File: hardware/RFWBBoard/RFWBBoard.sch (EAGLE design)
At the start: 122 parts, among them IC1 24LC025ST, J1 CON-71742-3003-BOT, M1 MOUNT-HOLE3.3, M2 MOUNT-HOLE3.3, M3 MOUNT-HOLE3.3, M4 MOUNT-HOLE3.3, M5 FIDUCIAL1X2, M6 FIDUCIAL1X2, M7 FIDUCIAL1X2, M8 FIDUCIAL1X2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

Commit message: - Logos - Gerber files - Pick and Place file - Assembly files
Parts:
- removed LOGO1: LOGO-ISIS-600MIL-10MM-AU, Logo:LOGO-ISIS-600MIL-10MM-AU
- removed LOGO2: LOGO-MARMOTE-600MIL-10MM-AU, Logo:LOGO-MARMOTE-600MIL-10MM-AU
- removed LOGO3: LOGO-VANDERBILT-600MIL-10MM-AU, Logo:LOGO-VANDERBILT-600MIL-10MM-AU
- added LOGO4: LOGO-ISIS-600MIL-10MM-SS, Logo:LOGO-ISIS-600MIL-10MM-SS
- added LOGO5: LOGO-VANDERBILT-600MIL-10MM-SS, Logo:LOGO-VANDERBILT-600MIL-10MM-SS
- added LOGO6: LOGO-MARMOTE-600MIL-10MM-SS, Logo:LOGO-MARMOTE-600MIL-10MM-SS
- added LOGO7: LOGO-RADIO-3-600MIL-10MM-SS, Logo:LOGO-RADIO-3-600MIL-10MM-SS
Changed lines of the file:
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@@
 <attribute name="REVIEWEREMAIL2" value="sandor.szilvasi@vanderbilt.edu"/>
 <attribute name="REVISION" value="A"/>
-<attribute name="TITLE" value="Radio Front-End Board"/>
+<attribute name="TITLE" value="Joshua"/>
 </attributes>
 <variantdefs>
@@
 <part name="RA00" library="RFWBBoard" deviceset="R" device="0402" value="DNP"/>
 <part name="RA01" library="RFWBBoard" deviceset="R" device="0402" value="DNP"/>
-<part name="LOGO1" library="Logo" deviceset="LOGO-ISIS-600MIL" device="-10MM-AU"/>
-<part name="LOGO2" library="Logo" deviceset="LOGO-MARMOTE-600MIL" device="-10MM-AU"/>
-<part name="LOGO3" library="Logo" deviceset="LOGO-VANDERBILT-600MIL" device="-10MM-AU"/>
 <part name="R1" library="RFWBBoard" deviceset="R" device="0402" value="4.7k"/>
 <part name="R2" library="RFWBBoard" deviceset="R" device="0402" value="4.7k"/>
@@
 <part name="C73" library="RFWBBoard" deviceset="C" device="0402" value="10nF"/>
 <part name="C71" library="RFWBBoard" deviceset="CPOL" device="2012" value="10uF"/>
+<part name="LOGO4" library="Logo" deviceset="LOGO-ISIS-600MIL" device="-10MM-SS"/>
+<part name="LOGO5" library="Logo" deviceset="LOGO-VANDERBILT-600MIL" device="-10MM-SS"/>
+<part name="LOGO6" library="Logo" deviceset="LOGO-MARMOTE-600MIL" device="-10MM-SS"/>
+<part name="LOGO7" library="Logo" deviceset="LOGO-RADIO-3-600MIL" device="-10MM-SS"/>
 </parts>
 <sheets>
 <sheet>
 <plain>
-<text x="53.34" y="116.84" size="10.16" layer="97">&gt;TITLE</text>
+<text x="99.06" y="116.84" size="10.16" layer="97">&gt;TITLE</text>
 <text x="38.1" y="101.6" size="5.08" layer="97">7.5-18 MHz wide 2.4-2.5 GHz/Baseband Radio Front-End</text>
 <text x="74.93" y="81.28" size="5.08" layer="97">http://marmote.googlecode.com</text>
@@
 <instance part="U$1" gate="G$1" x="0" y="0"/>
 <instance part="U$2" gate="G$1" x="81.28" y="0"/>
-<instance part="LOGO1" gate="G$1" x="119.38" y="53.34"/>
-<instance part="LOGO2" gate="G$1" x="152.4" y="53.34"/>
-<instance part="LOGO3" gate="G$1" x="86.36" y="53.34"/>
+<instance part="LOGO4" gate="G$1" x="104.14" y="53.34"/>
+<instance part="LOGO5" gate="G$1" x="73.66" y="53.34"/>
+<instance part="LOGO6" gate="G$1" x="134.62" y="53.34"/>
+<instance part="LOGO7" gate="G$1" x="165.1" y="53.34"/>
 </instances>
 <busses>

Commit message: - Gerber - BOM - README.txt - Schematic
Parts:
- C104: value NONE -> DNP
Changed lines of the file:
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@@
 <layer number="196" name="mValues" color="7" fill="1" visible="no" active="no"/>
 <layer number="199" name="EXTD_ERC" color="7" fill="1" visible="yes" active="yes"/>
-<layer number="200" name="200bmp" color="1" fill="10" visible="yes" active="yes"/>
+<layer number="200" name="200bmp" color="1" fill="10" visible="no" active="yes"/>
 <layer number="201" name="201bmp" color="2" fill="10" visible="yes" active="yes"/>
 <layer number="202" name="202bmp" color="3" fill="10" visible="yes" active="yes"/>
@@
 <part name="C103" library="RFWBBoard" deviceset="C" device="0402" value="100pF"/>
 <part name="C117" library="RFWBBoard" deviceset="C" device="0402" value="100nF"/>
-<part name="C104" library="RFWBBoard" deviceset="C" device="0402" value="NONE"/>
+<part name="C104" library="RFWBBoard" deviceset="C" device="0402" value="DNP"/>
 <part name="C106" library="RFWBBoard" deviceset="C" device="0402" value="100pF"/>
 <part name="C107" library="RFWBBoard" deviceset="C" device="0402" value="100pF"/>

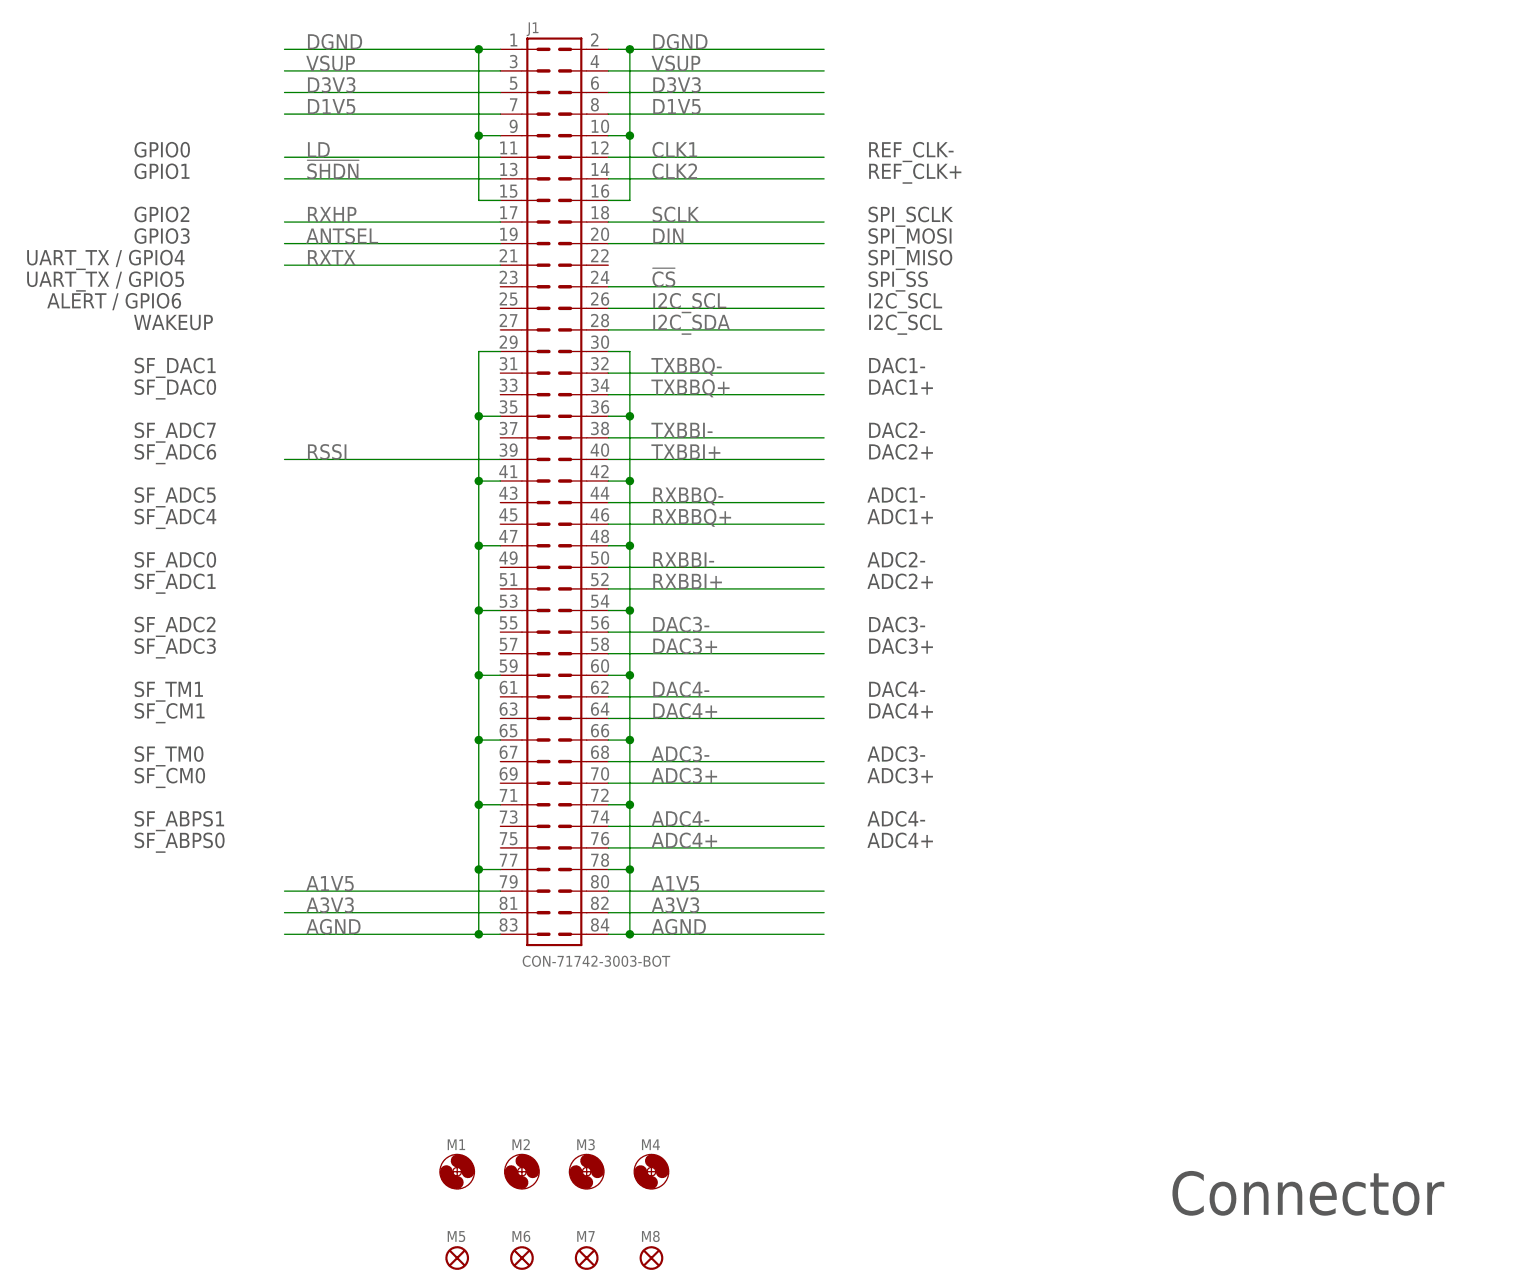
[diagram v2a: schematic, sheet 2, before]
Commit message: Modified signal name notes around connector.
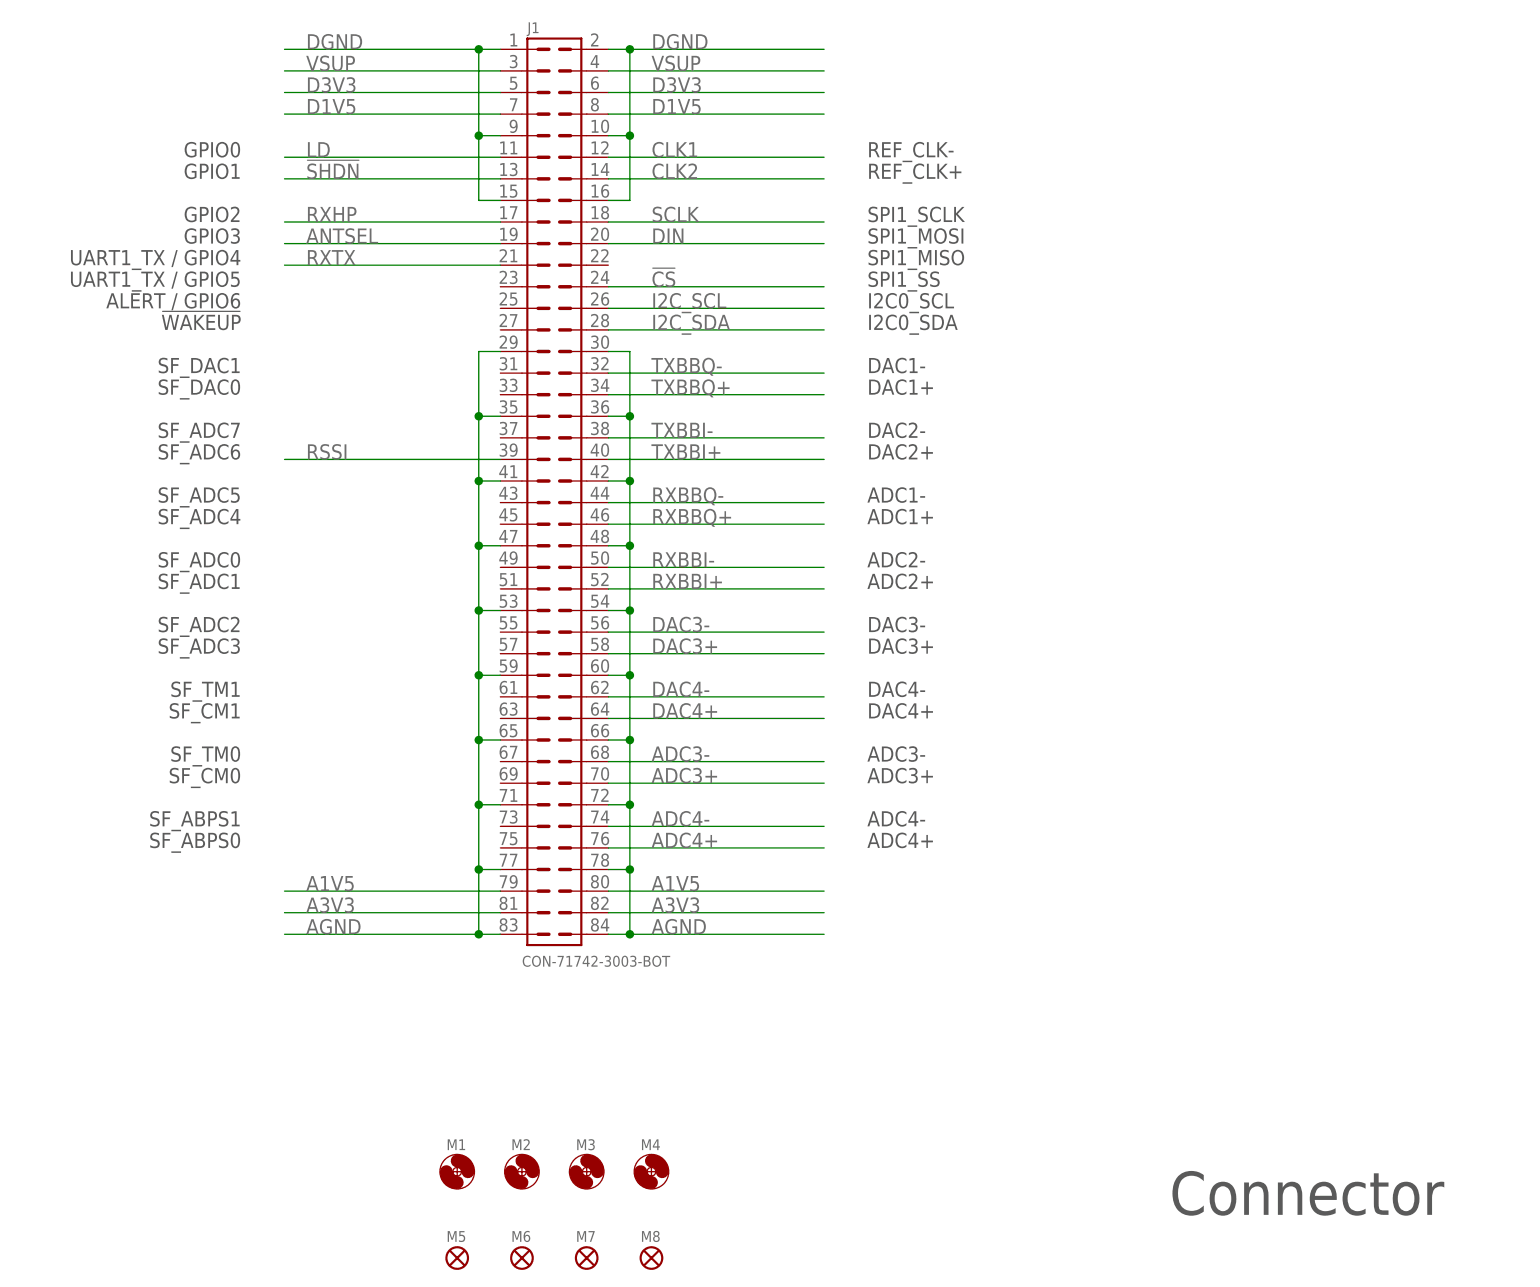
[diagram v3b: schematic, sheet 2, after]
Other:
- note added: "!WAKEUP"
- note added: "I2C0_SCL"
- note added: "I2C0_SDA"
- note added: "SPI1_MISO"
- note added: "SPI1_MOSI"
- note added: "SPI1_SCLK"
- note added: "SPI1_SS"
- note added: "UART1_TX / GPIO4"
- note added: "UART1_TX / GPIO5"
- note removed: "I2C_SCL"
- note removed: "SPI_MISO"
- note removed: "SPI_MOSI"
- note removed: "SPI_SCLK"
- note removed: "SPI_SS"
- note removed: "UART_TX / GPIO4"
- note removed: "UART_TX / GPIO5"
- note removed: "WAKEUP"
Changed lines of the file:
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@@
 <setting verticaltext="up"/>
 </settings>
-<grid distance="0.1" unitdist="inch" unit="inch" style="lines" multiple="1" display="no" altdistance="0.05" altunitdist="inch" altunit="inch"/>
+<grid distance="0.1" unitdist="inch" unit="inch" style="lines" multiple="1" display="no" altdistance="0.025" altunitdist="inch" altunit="inch"/>
 <layers>
 <layer number="1" name="Top" color="4" fill="1" visible="no" active="no"/>
@@
 <plain>
 <text x="190.5" y="20.32" size="5.08" layer="97">&gt;PAGE2</text>
-<text x="68.58" y="109.22" size="1.778" layer="97">SF_ADC6</text>
-<text x="68.58" y="137.16" size="1.778" layer="97">GPIO2</text>
-<text x="68.58" y="134.62" size="1.778" layer="97">GPIO3</text>
-<text x="68.58" y="142.24" size="1.778" layer="97">GPIO1</text>
-<text x="68.58" y="144.78" size="1.778" layer="97">GPIO0</text>
-<text x="55.88" y="132.08" size="1.778" layer="97">UART_TX / GPIO4</text>
-<text x="154.94" y="137.16" size="1.778" layer="97">SPI_SCLK</text>
-<text x="154.94" y="134.62" size="1.778" layer="97">SPI_MOSI</text>
-<text x="154.94" y="132.08" size="1.778" layer="97">SPI_MISO</text>
-<text x="154.94" y="129.54" size="1.778" layer="97">SPI_SS</text>
-<text x="154.94" y="127" size="1.778" layer="97">I2C_SCL</text>
-<text x="154.94" y="124.46" size="1.778" layer="97">I2C_SCL</text>
+<text x="81.28" y="109.22" size="1.778" layer="97" rot="MR0">SF_ADC6</text>
+<text x="81.28" y="137.16" size="1.778" layer="97" rot="MR0">GPIO2</text>
+<text x="81.28" y="134.62" size="1.778" layer="97" rot="MR0">GPIO3</text>
+<text x="81.28" y="142.24" size="1.778" layer="97" rot="MR0">GPIO1</text>
+<text x="81.28" y="144.78" size="1.778" layer="97" rot="MR0">GPIO0</text>
+<text x="81.28" y="132.08" size="1.778" layer="97" rot="MR0">UART1_TX / GPIO4</text>
+<text x="154.94" y="137.16" size="1.778" layer="97">SPI1_SCLK</text>
+<text x="154.94" y="134.62" size="1.778" layer="97">SPI1_MOSI</text>
+<text x="154.94" y="132.08" size="1.778" layer="97">SPI1_MISO</text>
+<text x="154.94" y="129.54" size="1.778" layer="97">SPI1_SS</text>
+<text x="154.94" y="127" size="1.778" layer="97">I2C0_SCL</text>
+<text x="154.94" y="124.46" size="1.778" layer="97">I2C0_SDA</text>
 <text x="154.94" y="119.38" size="1.778" layer="97">DAC1-</text>
 <text x="154.94" y="116.84" size="1.778" layer="97">DAC1+</text>
@@
 <text x="154.94" y="144.78" size="1.778" layer="97">REF_CLK-</text>
 <text x="154.94" y="142.24" size="1.778" layer="97">REF_CLK+</text>
-<text x="55.88" y="129.54" size="1.778" layer="97">UART_TX / GPIO5</text>
-<text x="58.42" y="127" size="1.778" layer="97">ALERT / GPIO6</text>
-<text x="68.58" y="124.46" size="1.778" layer="97">WAKEUP</text>
-<text x="68.58" y="111.76" size="1.778" layer="97">SF_ADC7</text>
-<text x="68.58" y="119.38" size="1.778" layer="97">SF_DAC1</text>
-<text x="68.58" y="116.84" size="1.778" layer="97">SF_DAC0</text>
-<text x="68.58" y="104.14" size="1.778" layer="97">SF_ADC5</text>
-<text x="68.58" y="101.6" size="1.778" layer="97">SF_ADC4</text>
-<text x="68.58" y="96.52" size="1.778" layer="97">SF_ADC0</text>
-<text x="68.58" y="93.98" size="1.778" layer="97">SF_ADC1</text>
-<text x="68.58" y="88.9" size="1.778" layer="97">SF_ADC2</text>
-<text x="68.58" y="86.36" size="1.778" layer="97">SF_ADC3</text>
-<text x="68.58" y="81.28" size="1.778" layer="97">SF_TM1</text>
-<text x="68.58" y="78.74" size="1.778" layer="97">SF_CM1</text>
-<text x="68.58" y="73.66" size="1.778" layer="97">SF_TM0</text>
-<text x="68.58" y="71.12" size="1.778" layer="97">SF_CM0</text>
-<text x="68.58" y="66.04" size="1.778" layer="97">SF_ABPS1</text>
-<text x="68.58" y="63.5" size="1.778" layer="97">SF_ABPS0</text>
+<text x="81.28" y="129.54" size="1.778" layer="97" rot="MR0">UART1_TX / GPIO5</text>
+<text x="81.28" y="127" size="1.778" layer="97" rot="MR0">ALERT / GPIO6</text>
+<text x="81.28" y="124.46" size="1.778" layer="97" rot="MR0">!WAKEUP</text>
+<text x="81.28" y="111.76" size="1.778" layer="97" rot="MR0">SF_ADC7</text>
+<text x="81.28" y="119.38" size="1.778" layer="97" rot="MR0">SF_DAC1</text>
+<text x="81.28" y="116.84" size="1.778" layer="97" rot="MR0">SF_DAC0</text>
+<text x="81.28" y="104.14" size="1.778" layer="97" rot="MR0">SF_ADC5</text>
+<text x="81.28" y="101.6" size="1.778" layer="97" rot="MR0">SF_ADC4</text>
+<text x="81.28" y="96.52" size="1.778" layer="97" rot="MR0">SF_ADC0</text>
+<text x="81.28" y="93.98" size="1.778" layer="97" rot="MR0">SF_ADC1</text>
+<text x="81.28" y="88.9" size="1.778" layer="97" rot="MR0">SF_ADC2</text>
+<text x="81.28" y="86.36" size="1.778" layer="97" rot="MR0">SF_ADC3</text>
+<text x="81.28" y="81.28" size="1.778" layer="97" rot="MR0">SF_TM1</text>
+<text x="81.28" y="78.74" size="1.778" layer="97" rot="MR0">SF_CM1</text>
+<text x="81.28" y="73.66" size="1.778" layer="97" rot="MR0">SF_TM0</text>
+<text x="81.28" y="71.12" size="1.778" layer="97" rot="MR0">SF_CM0</text>
+<text x="81.28" y="66.04" size="1.778" layer="97" rot="MR0">SF_ABPS1</text>
+<text x="81.28" y="63.5" size="1.778" layer="97" rot="MR0">SF_ABPS0</text>
 </plain>
 <instances>

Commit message: - Layout updated
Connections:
- net AGND: no longer C123.2, C124.2, C125.2, C126.2, C127.2, C128.2, C129.2, C130.2, C131.2, U8.GND, U9.VEE, X3.GND
- net DGND: now also C123.2, C124.2, C125.2, C126.2, C127.2, C128.2, C129.2, C130.2, C131.2, U8.GND, U9.VEE, X3.GND
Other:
- moved on the sheet: C118, C119, C120, C121, C122, C123, C124, C125, C126, C127, C128, C129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
